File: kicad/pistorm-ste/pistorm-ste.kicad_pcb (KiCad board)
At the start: 4 copper layers, 27 parts, among them J1 Raspberry_Pi_2_3, U1 SN54CBTD3384, U2 SN74LVC16373, U3 SN74LVC16373, U4 EPM240T100, U5 SN74LVC16373, U6 SN74LVC16373, U7 SN54CBTD3384, U8 LM1117-3.3

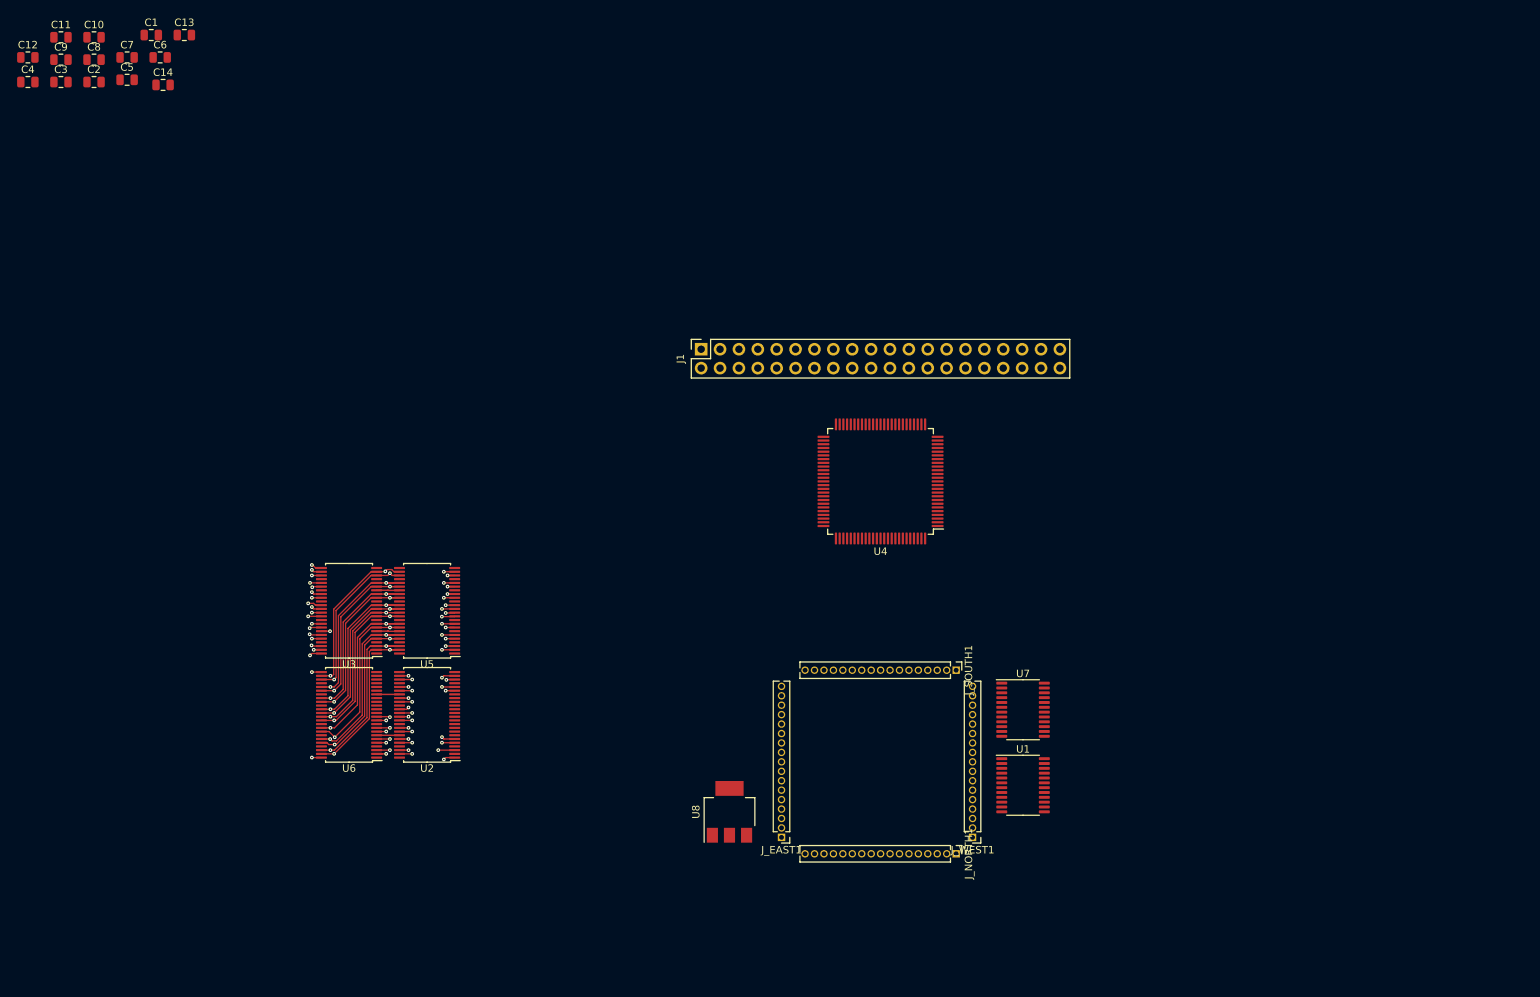
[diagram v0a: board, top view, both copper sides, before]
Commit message: Upgrade to Kicad6 happened. Need to test measurements before routing as don't know about layout yet.
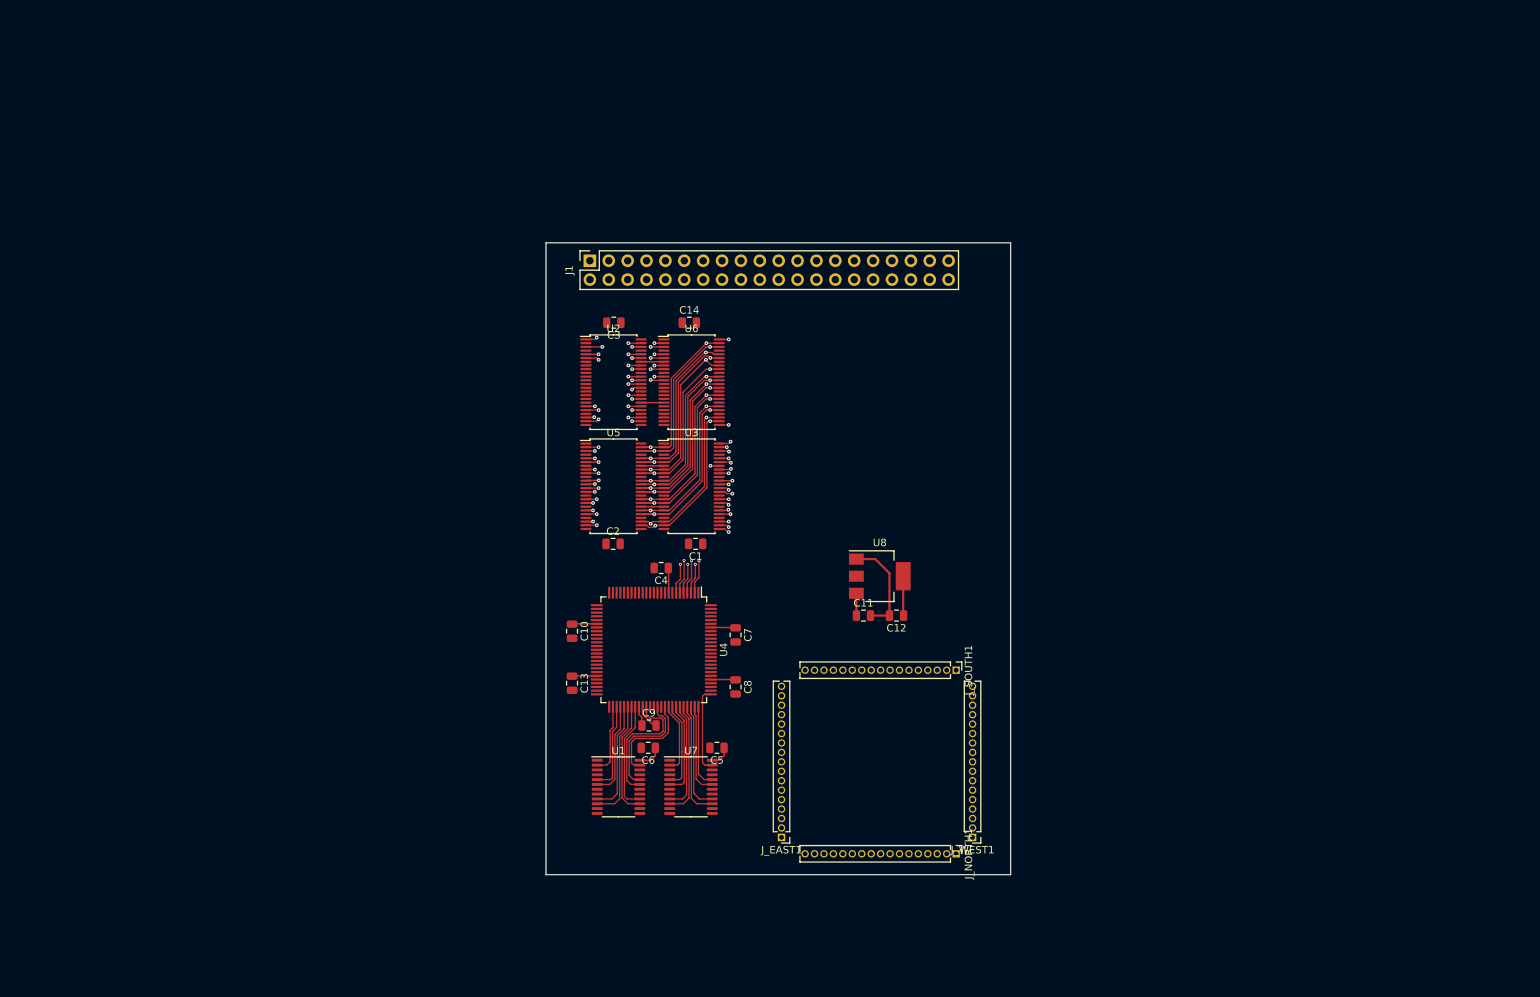
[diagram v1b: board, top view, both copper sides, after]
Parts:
- moved C12 138.9 mm to (151.3, 120.1), turned to 180 degrees
- moved C11 133.1 mm to (146.8, 120.1)
- moved C8 120.7 mm to (129.6, 129.7), turned to -90 degrees
- moved C5 119.9 mm to (127.1, 137.9), turned to 180 degrees
- moved C9 119.5 mm to (118.0, 134.9)
- moved C6 113.7 mm to (117.9, 137.9), turned to 180 degrees
- moved C7 112.9 mm to (129.6, 122.7), turned to -90 degrees
- moved C4 107.4 mm to (119.6, 113.7), turned to 180 degrees
- moved C10 102.6 mm to (107.6, 122.2), turned to -90 degrees
- moved C13 101.6 mm to (107.6, 129.2), turned to -90 degrees
- moved C1 100.2 mm to (124.2, 110.4), turned to 180 degrees
- moved C2 93.5 mm to (113.1, 110.4)
- moved C3 81.1 mm to (113.2, 80.7), turned to 180 degrees
- moved C14 77.7 mm to (123.4, 80.7)
- moved U6 64.2 mm to (123.7, 88.7), turned to 0 degrees
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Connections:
- J1 pad 1: Net-(J1-Pad1) -> unconnected-(J1-Pad1)
- J1 pad 17: Net-(J1-Pad17) -> unconnected-(J1-Pad17)
- J_SOUTH1 pad 5: Net-(J_SOUTH1-Pad5) -> unconnected-(J_SOUTH1-Pad5)
- J_WEST1 pad 9: Net-(J_WEST1-Pad9) -> unconnected-(J_WEST1-Pad9)
- U1 pad 16: /IPL2_3 -> /IPL1_3
- U1 pad 17: /IPL2 -> /IPL1
- U1 pad 18: /IPL1 -> /IPL2
- U1 pad 19: /IPL1_3 -> /IPL2_3
- U2 pad 2: Net-(U2-Pad2) -> unconnected-(U2-Pad2)
- U4 pad 1: Net-(U4-Pad1) -> unconnected-(U4-Pad1)
- U4 pad 100: Net-(U4-Pad100) -> unconnected-(U4-Pad100)
- U4 pad 37: Net-(U4-Pad37) -> unconnected-(U4-Pad37)
- U4 pad 39: Net-(U4-Pad39) -> unconnected-(U4-Pad39)
- U4 pad 51: Net-(U4-Pad51) -> unconnected-(U4-Pad51)
- U4 pad 77: Net-(U4-Pad77) -> unconnected-(U4-Pad77)
- U4 pad 78: Net-(U4-Pad78) -> unconnected-(U4-Pad78)
- U4 pad 81: Net-(U4-Pad81) -> unconnected-(U4-Pad81)
- U4 pad 82: Net-(U4-Pad82) -> unconnected-(U4-Pad82)
- U4 pad 83: Net-(U4-Pad83) -> unconnected-(U4-Pad83)
- U4 pad 84: Net-(U4-Pad84) -> unconnected-(U4-Pad84)
- U4 pad 85: Net-(U4-Pad85) -> unconnected-(U4-Pad85)
- U4 pad 86: Net-(U4-Pad86) -> unconnected-(U4-Pad86)
- U4 pad 87: Net-(U4-Pad87) -> unconnected-(U4-Pad87)
- U4 pad 88: Net-(U4-Pad88) -> unconnected-(U4-Pad88)
- U4 pad 89: Net-(U4-Pad89) -> unconnected-(U4-Pad89)
- U4 pad 90: Net-(U4-Pad90) -> unconnected-(U4-Pad90)
- U4 pad 91: Net-(U4-Pad91) -> unconnected-(U4-Pad91)
- U4 pad 92: Net-(U4-Pad92) -> unconnected-(U4-Pad92)
- U4 pad 95: Net-(U4-Pad95) -> unconnected-(U4-Pad95)
- U4 pad 96: Net-(U4-Pad96) -> unconnected-(U4-Pad96)
- U4 pad 97: Net-(U4-Pad97) -> unconnected-(U4-Pad97)
- U4 pad 98: Net-(U4-Pad98) -> unconnected-(U4-Pad98)
- U4 pad 99: Net-(U4-Pad99) -> unconnected-(U4-Pad99)
- U6 pad 13: Net-(U6-Pad13) -> unconnected-(U6-Pad13)
- U6 pad 14: Net-(U6-Pad14) -> unconnected-(U6-Pad14)
- U6 pad 16: Net-(U6-Pad16) -> unconnected-(U6-Pad16)
- U6 pad 17: Net-(U6-Pad17) -> unconnected-(U6-Pad17)
- U6 pad 19: Net-(U6-Pad19) -> unconnected-(U6-Pad19)
- U6 pad 20: Net-(U6-Pad20) -> unconnected-(U6-Pad20)
- U6 pad 22: Net-(U6-Pad22) -> unconnected-(U6-Pad22)
- U6 pad 23: Net-(U6-Pad23) -> unconnected-(U6-Pad23)
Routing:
- net +3V3: track 13.5 -> 38.2 mm
- net /SD0: track 36.5 -> 59.4 mm, vias 3 -> 4
- net /SD1: track 37.0 -> 58.6 mm, vias 3 -> 4
- net /SD2: track 37.8 -> 58.8 mm, vias 3 -> 4
- net /SD3: track 38.2 -> 58.1 mm, vias 3 -> 4
- net /SD4: track 39.3 -> 58.7 mm, vias 3 -> 4
- net /SD5: track 38.8 -> 57.0 mm, vias 3 -> 4
- net /IPL2_3: track 0.00 -> 17.9 mm
- net GND: track 0.00 -> 16.9 mm
- net /IPL0_3: track 0.00 -> 16.1 mm
- net /FC1_3: track 0.00 -> 15.8 mm
- net /AS_3: track 0.00 -> 15.7 mm
- net /BG_3: track 0.00 -> 15.5 mm
- net /FC2_3: track 0.00 -> 15.5 mm
- net /BERR_3: track 0.00 -> 15.0 mm
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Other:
- board outline added: 62.5 x 85 mm
- net class Default removed
- net class PWR removed

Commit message: Trying a different layout
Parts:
- moved U2 103.5 mm to (216.7, 91.4)
- moved U3 103.5 mm to (227.2, 105.4)
- moved U5 103.5 mm to (216.7, 105.4)
- moved U6 103.5 mm to (227.2, 91.4)
- moved C1 103.5 mm to (227.7, 113.1)
- moved C10 103.5 mm to (211.1, 124.9)
- moved C13 103.5 mm to (211.1, 131.9)
- moved C14 103.5 mm to (226.9, 83.4)
- moved C2 103.5 mm to (216.6, 113.1)
- moved C3 103.5 mm to (216.7, 83.4)
- moved C4 103.5 mm to (223.1, 116.4)
- moved C5 103.5 mm to (230.6, 140.6)
- moved C6 103.5 mm to (221.3, 140.6)
- moved C7 103.5 mm to (233.1, 125.4)
- moved C8 103.5 mm to (233.1, 132.4)
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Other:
- board size 62.5 x 85 mm -> 107.5 x 39 mm

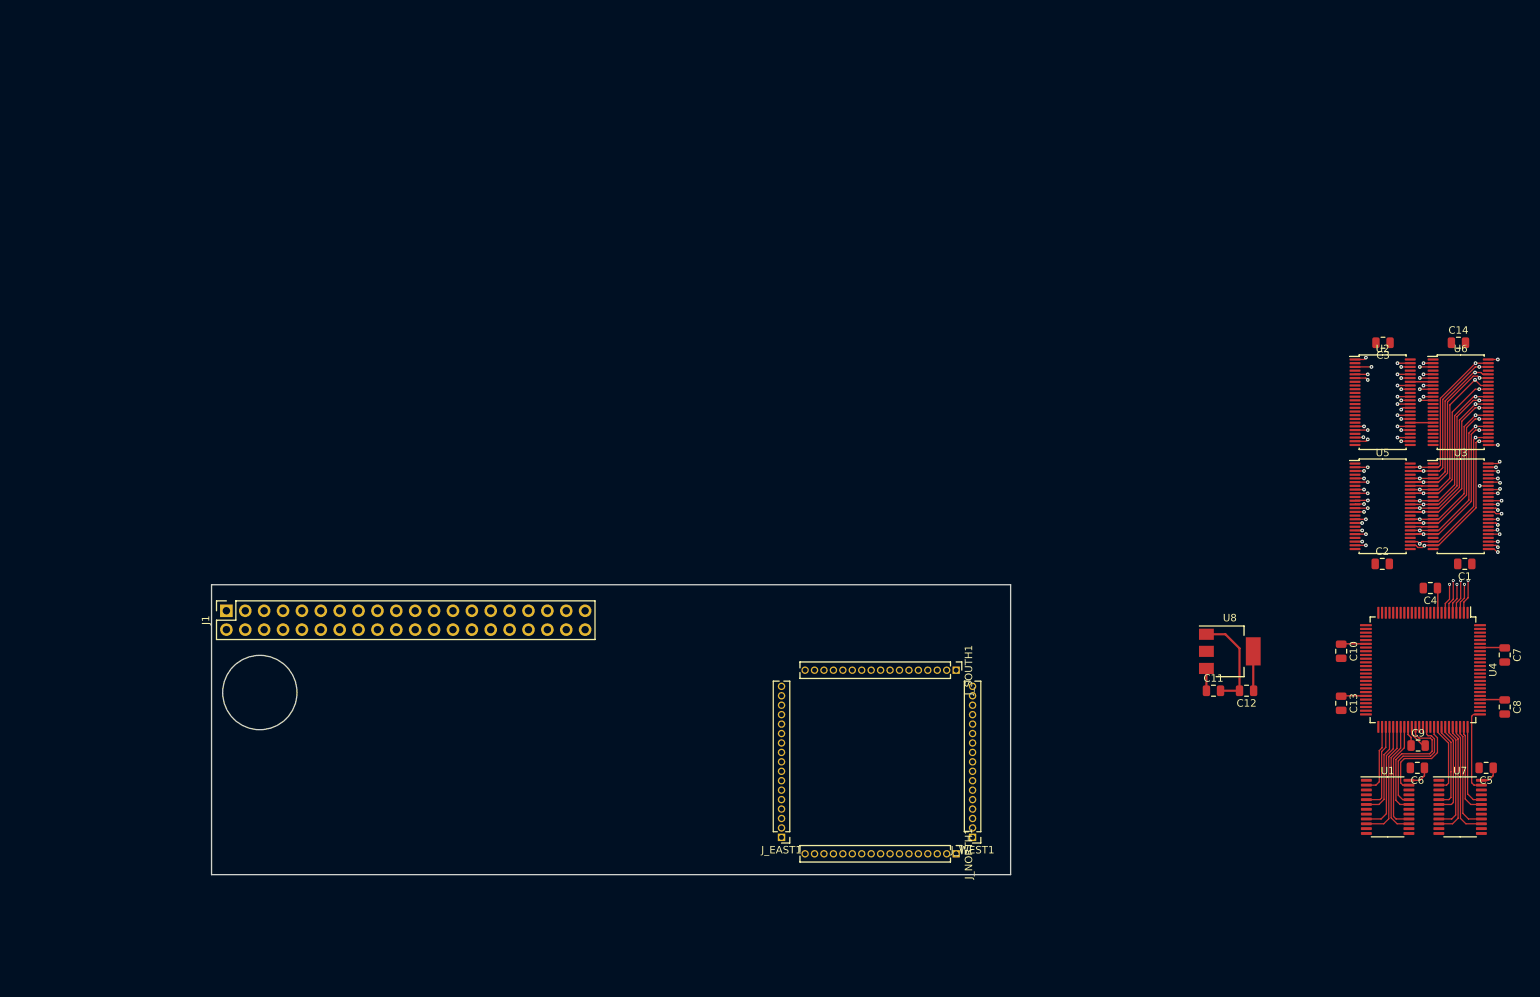
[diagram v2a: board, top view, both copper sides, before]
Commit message: Working on tightening the gap to the two level shifters and the CPU pins
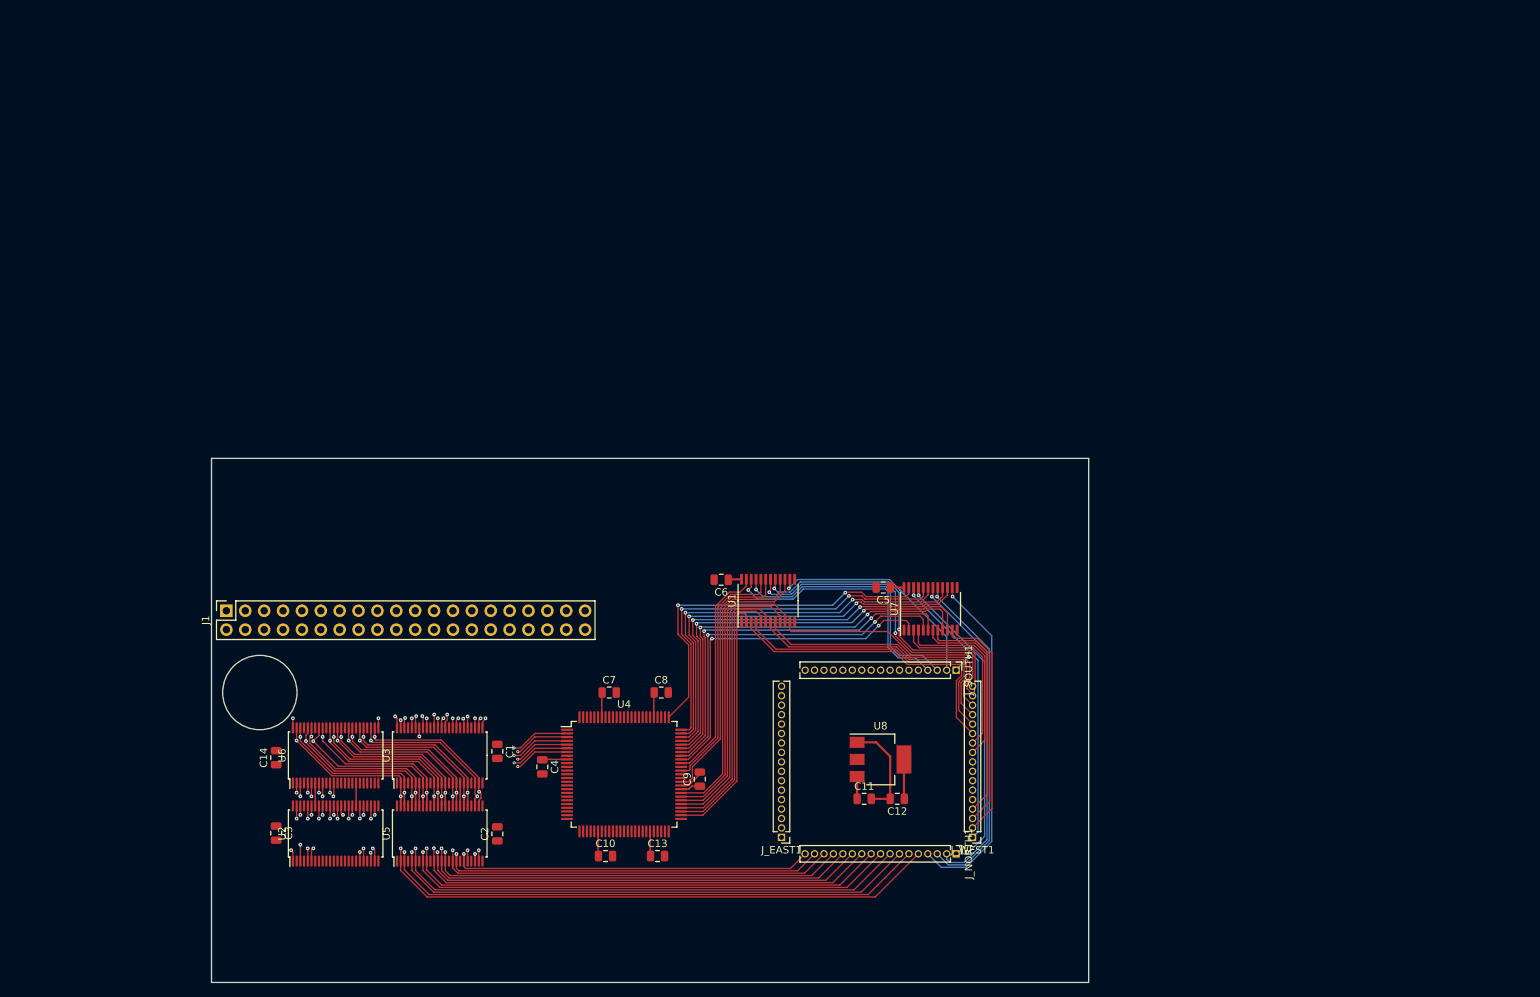
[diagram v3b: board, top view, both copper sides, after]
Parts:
- moved C14 168.6 mm to (67.8, 139.2), turned to 90 degrees
- moved C3 162.9 mm to (67.8, 149.4), turned to -90 degrees
- moved U6 158.6 mm to (75.8, 138.9), turned to 90 degrees
- moved U2 152.3 mm to (75.8, 149.4), turned to 90 degrees
- moved U3 141.4 mm to (89.8, 138.9), turned to 90 degrees
- moved U5 134.3 mm to (89.8, 149.4), turned to 90 degrees
- moved C1 132.6 mm to (97.6, 138.4), turned to -90 degrees
- moved C2 124.5 mm to (97.6, 149.5), turned to 90 degrees
- moved C4 121.9 mm to (103.6, 140.4), turned to -90 degrees
- moved C7 120.6 mm to (112.6, 130.4), turned to 0 degrees
- moved C8 113.5 mm to (119.6, 130.4), turned to 0 degrees
- moved U4 108.4 mm to (114.6, 141.4), turned to 0 degrees
- moved C10 102.7 mm to (112.1, 152.4), turned to 0 degrees
- moved C6 97.0 mm to (127.7, 115.3)
- moved C9 96.7 mm to (124.8, 142.1), turned to 90 degrees
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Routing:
- net /D0: track 21.5 -> 96.3 mm
- net /D1: track 22.3 -> 95.0 mm
- net /D2: track 22.7 -> 92.9 mm
- net /D3: track 23.5 -> 91.7 mm
- net /D4: track 24.0 -> 89.6 mm
- net /D5: track 22.6 -> 86.1 mm
- net /D6: track 23.2 -> 84.2 mm
- net /D7: track 21.3 -> 80.4 mm
- net /D8: track 21.3 -> 78.3 mm
- net /D9: track 23.1 -> 78.1 mm
- net /D10: track 22.6 -> 74.8 mm
- net /D11: track 22.4 -> 72.6 mm
- net /D12: track 22.8 -> 70.4 mm
- net /AS: track 0.00 -> 47.1 mm, vias 0 -> 1
- net /UDS: track 0.00 -> 46.0 mm, vias 0 -> 1
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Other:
- board size 107.5 x 39 mm -> 118 x 70.5 mm
